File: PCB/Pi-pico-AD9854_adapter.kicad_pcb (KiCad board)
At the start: 2 copper layers, 38.7 x 80 mm, 15 parts, among them J1 Conn_02x20_Odd_Even, J2 TYPE-C-31-M-12, J3 Conn_01x01_Male, J4 Screw_Terminal_01x02, U1 Pico, U2 LM3940IMP-3.3, U3 DMG2305UX-13

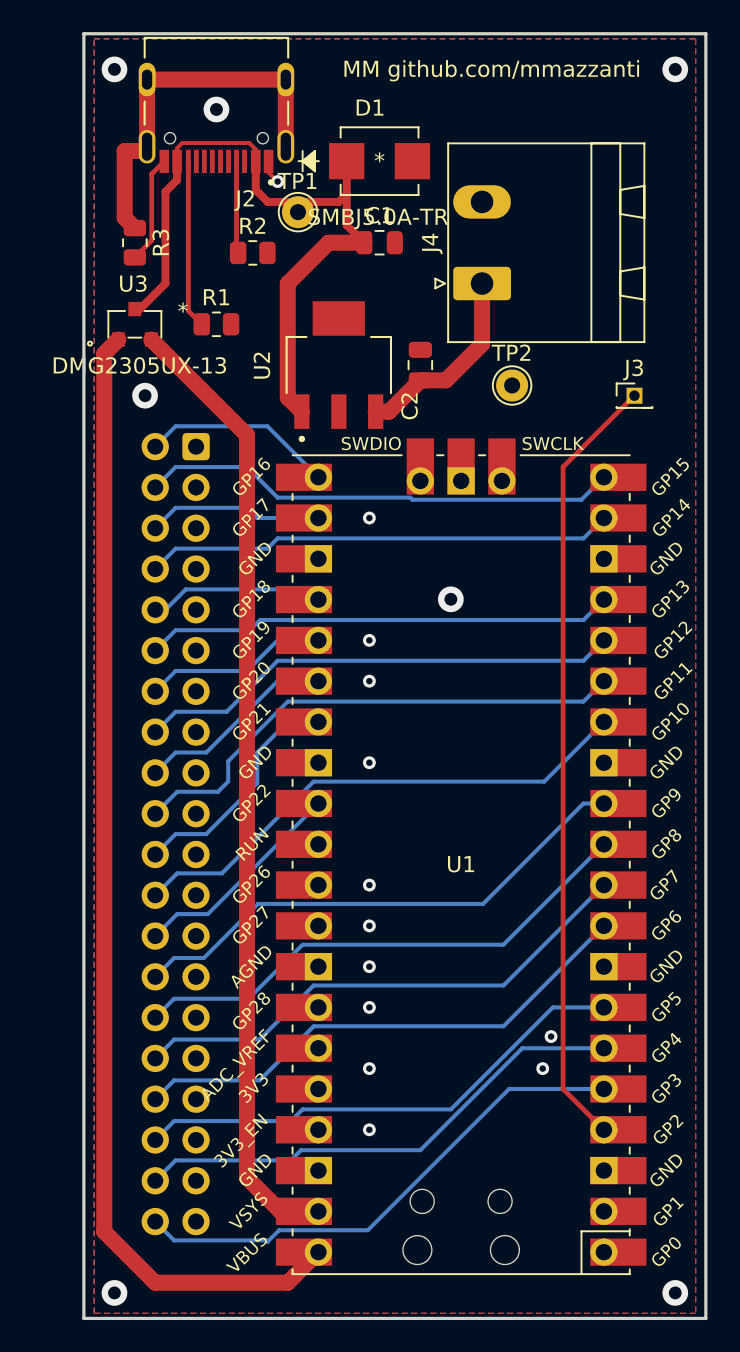
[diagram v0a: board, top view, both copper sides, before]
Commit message: V1.0_beta prototype. Firwmare fixes
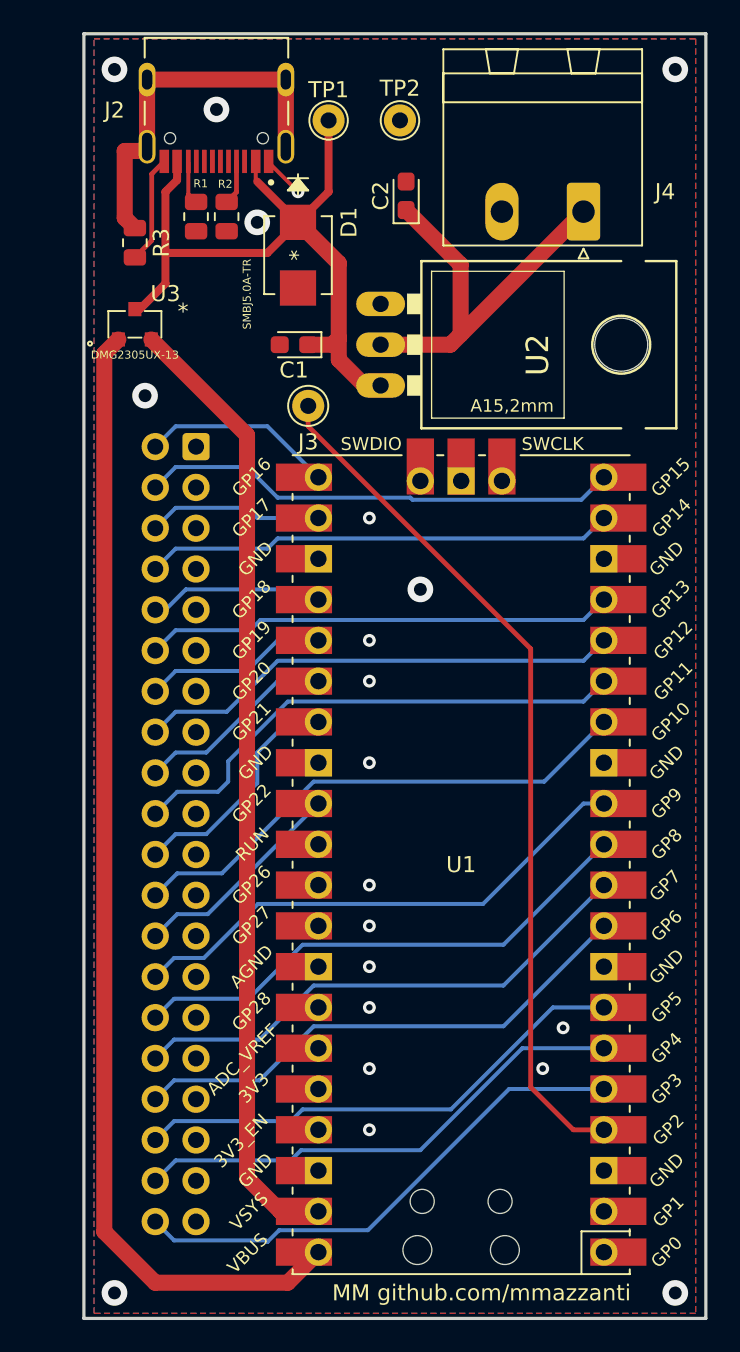
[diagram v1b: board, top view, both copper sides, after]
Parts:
- C1: value 0.47 uF -> 10uF; footprint Capacitor_SMD:C_0805_2012Metric -> Capacitor_Tantalum_SMD:CP_EIA-2012-12_Kemet-R
- C2: value 33 uF -> 10uF; footprint Capacitor_SMD:C_0805_2012Metric -> Capacitor_Tantalum_SMD:CP_EIA-2012-12_Kemet-R
- D1: footprint MM_ftprnt:SMBJ5.0A-TR -> SMBJ5-0A-TR:SMBJ5.0A-TR
- J2: footprint MM_ftprnt:HRO_TYPE-C-31-M-12 -> TYPE-C-31-M-12:HRO_TYPE-C-31-M-12
- J3: footprint Connector_PinHeader_1.27mm:PinHeader_1x01_P1.27mm_Vertical -> Connector_Pin:Pin_D1.0mm_L10.0mm
- U1: footprint MM_ftprnt:RPi_Pico_SMD_TH -> MCU_RaspberryPi_and_Boards:RPi_Pico_SMD_TH
- U2: value LM3940IMP-3.3 -> LT1086-3.3; footprint MM_ftprnt:SOT230P700X180-4N -> LT1086:LT1086
- U3: footprint MM_ftprnt:DMG2305UX-13 -> footprints:DMG2305UX-13
- moved J3 20.3 mm to (117.5, 38.1)
- moved TP2 17.9 mm to (123.2, 20.3)
- moved C2 10.6 mm to (123.6, 25.0)
- moved C1 8.29 mm to (116.6, 34.3), turned to 180 degrees
- moved D1 7.75 mm to (116.8, 28.7), turned to -90 degrees
- moved J4 7.74 mm to (134.6, 26.0), turned to 180 degrees
- moved R1 6.83 mm to (110.5, 26.3), turned to -90 degrees
- moved U2 6.54 mm to (125.8, 34.3), turned to -90 degrees
- moved TP1 6.02 mm to (118.7, 20.3)
- moved R2 2.79 mm to (112.4, 26.3), turned to -90 degrees
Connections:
- U2 pad 1: +5V -> GND
- U2 pad 2: GND -> +3V3
- U2 pad 3: +3V3 -> +5V
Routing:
- net +3V3: track 12.1 -> 25.2 mm
- net Net-(J2-PadB5): track 10.5 -> 2.72 mm
- net FSK/BPSK: track 48.6 -> 53.8 mm
- net Net-(J2-PadA5): track 5.74 -> 2.78 mm
- net +5V: track 44.9 -> 46.5 mm
- net GND: track 8.30 -> 9.38 mm, vias 20 -> 21
